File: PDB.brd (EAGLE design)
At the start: 125.9 x 103 mm, 73 parts

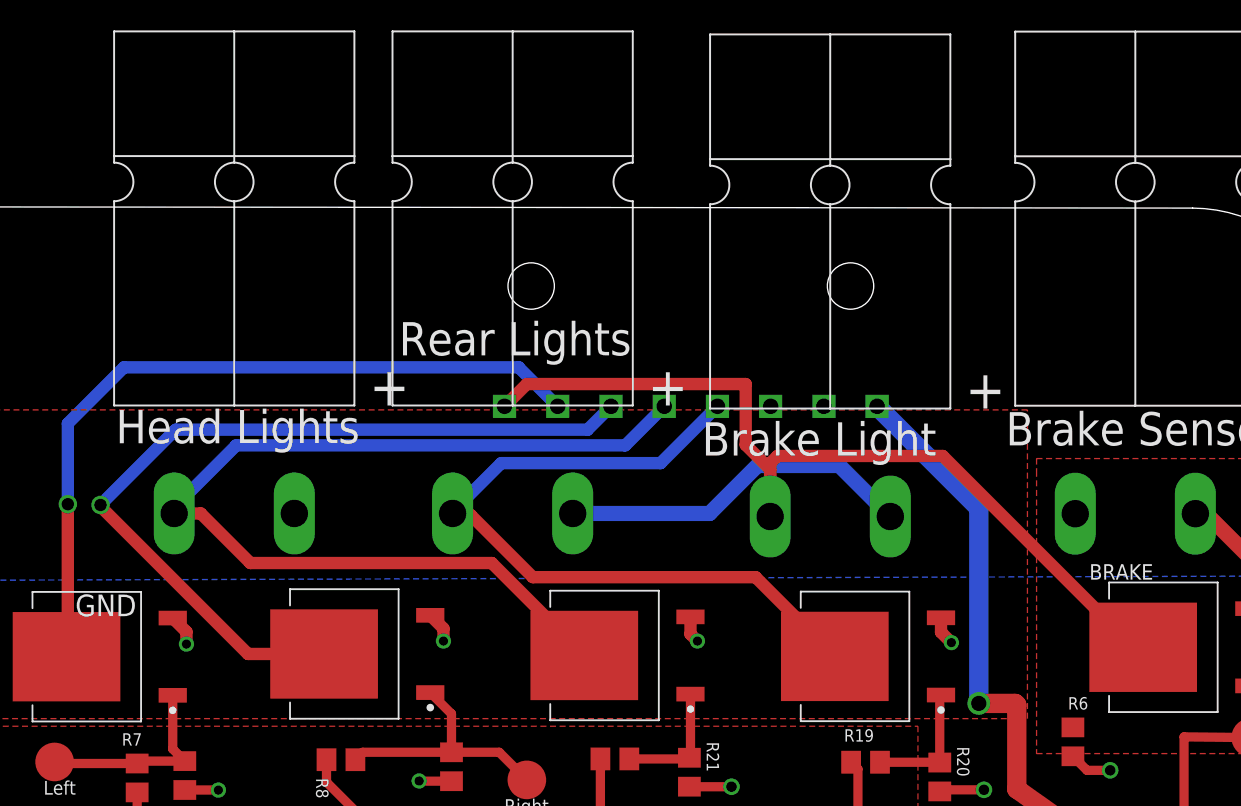
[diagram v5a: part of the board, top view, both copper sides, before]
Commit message: Deleted most Anderson connectors. Brake sensor waiting to be modified
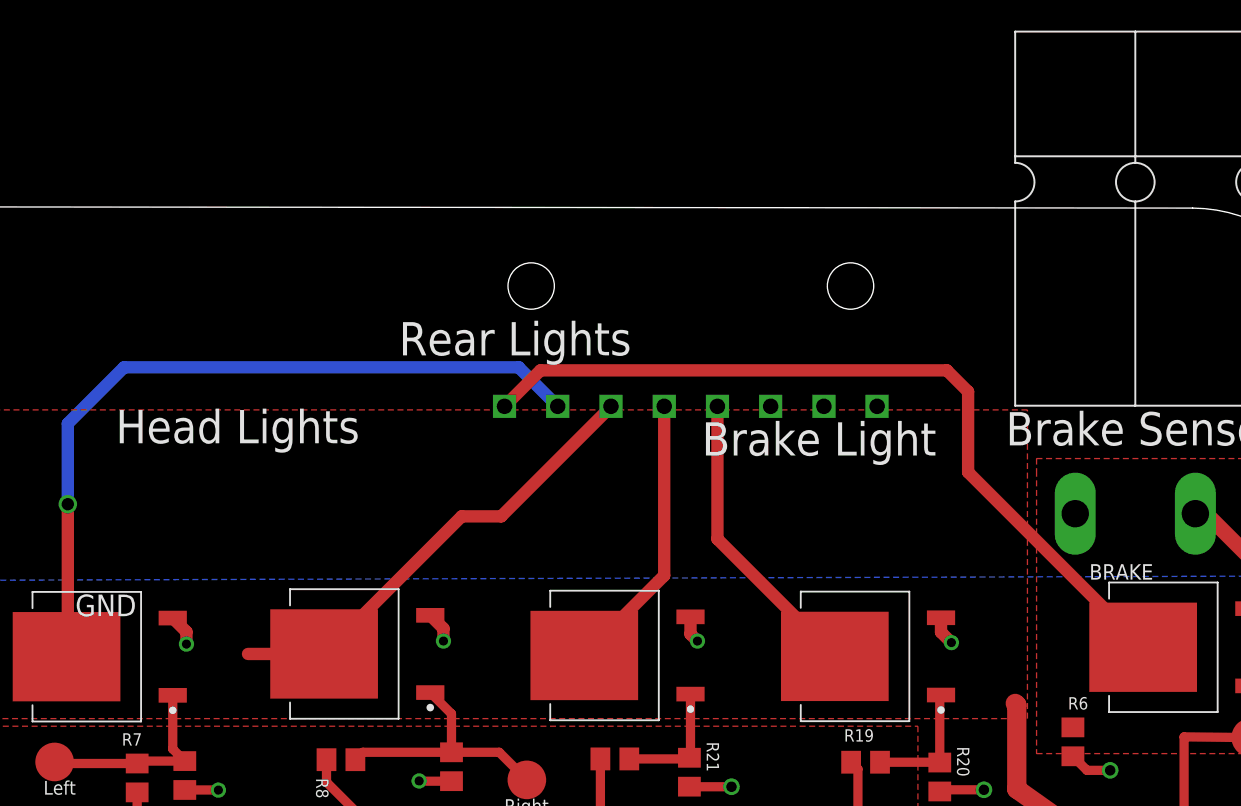
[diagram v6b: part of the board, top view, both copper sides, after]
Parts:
- removed BRAKE_OUT, HEADLIGHTS_OUT, REARLIGHTS_OUT: POWERPOLE_POWER25A_HORIZONTAL_G2, powerpoles:POWERPOLE_PAIR_25A_HORIZ_G2
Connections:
- removed net V+: BRAKE_OUT.RED, REARLIGHTS_OUT.RED
- net BRAKE_SIG: no longer BRAKE_OUT.BLACK
- net HEADLIGHT_SIG: no longer HEADLIGHTS_OUT.BLACK
- net REARLIGHT_SIG: no longer REARLIGHTS_OUT.BLACK
- net VDD: no longer HEADLIGHTS_OUT.RED
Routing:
- net HEADLIGHT_SIG: track 66.2 -> 18.6 mm
- net REARLIGHT_SIG: track 49.4 -> 19.6 mm
- net VDD: track 44.8 -> 20.1 mm, vias 1 -> 0
- net HAZ_R_SIG: track 58.4 -> 33.9 mm, vias 1 -> 0
- net V+: track 23.6 -> 0.00 mm
- net BRAKE_SIG: track 59.3 -> 53.6 mm
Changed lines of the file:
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@@
 <drawing>
 <settings>
-<setting alwaysvectorfont="yes"/>
+<setting alwaysvectorfont="no"/>
 <setting verticaltext="up"/>
 </settings>
@@
 <element name="ADD1" library="master_library" package="TO254P1054X240-3" package3d_urn="urn:adsk.eagle:package:8893803/1" value="NCV8405ADPAK-3PIN" x="56.654" y="68.958" smashed="yes" rot="R270"/>
 <element name="WIPER_OUT" library="powerpoles" package="POWERPOLE_PAIR_25A_HORIZ_G2" value="POWERPOLE_POWER25A_HORIZONTAL_G2" x="35.64" y="51.84" smashed="yes" rot="R180"/>
-<element name="BRAKE_OUT" library="powerpoles" package="POWERPOLE_PAIR_25A_HORIZ_G2" value="POWERPOLE_POWER25A_HORIZONTAL_G2" x="96.232" y="133.49" smashed="yes"/>
-<element name="HEADLIGHTS_OUT" library="powerpoles" package="POWERPOLE_PAIR_25A_HORIZ_G2" value="POWERPOLE_POWER25A_HORIZONTAL_G2" x="57.044" y="133.69" smashed="yes"/>
-<element name="REARLIGHTS_OUT" library="powerpoles" package="POWERPOLE_PAIR_25A_HORIZ_G2" value="POWERPOLE_POWER25A_HORIZONTAL_G2" x="75.35" y="133.69" smashed="yes"/>
 <element name="BRAKE" library="master_library" package="TO254P1054X240-3" package3d_urn="urn:adsk.eagle:package:8893803/1" value="NCV8405ADPAK-3PIN" x="118.994" y="117.792" smashed="yes" rot="R180">
 <attribute name="NAME" x="113.26755" y="122.239" size="1.017" layer="25" font="vector" rot="SR0"/>
@@
 <signals>
 <signal name="VDD">
-<contactref element="HEADLIGHTS_OUT" pad="RED"/>
 <contactref element="C10" pad="+"/>
 <contactref element="D1" pad="C"/>
@@
 <wire x1="108.5" y1="108.461690625" x2="108.5" y2="114" width="1.27" layer="1"/>
 <wire x1="108.5" y1="114" x2="108.4" y2="114.1" width="1.27" layer="1"/>
-<wire x1="108.4" y1="114.1" x2="106" y2="114.1" width="1.27" layer="1"/>
 <wire x1="118.24" y1="101.56" x2="118.236340625" y2="101.57038125" width="1.27" layer="1"/>
-<via x="106" y="114.1" extent="1-16" drill="1"/>
 <contactref element="U$2" pad="P$1"/>
 <contactref element="U$2" pad="P$2"/>
@@
 <contactref element="LIGHTS" pad="P7"/>
 <contactref element="LIGHTS" pad="P8"/>
-<wire x1="106" y1="114.1" x2="106" y2="126.952" width="1.27" layer="16"/>
-<wire x1="106" y1="126.952" x2="99.316" y2="133.636" width="1.27" layer="16"/>
 </signal>
 <signal name="N$19">
@@
 </signal>
 <signal name="BRAKE_SIG">
-<contactref element="BRAKE" pad="3"/>
-<contactref element="BRAKE_OUT" pad="BLACK"/>
 <contactref element="LIGHTS" pad="P1"/>
-<wire x1="103.631" y1="130.37" x2="92.762" y2="130.37" width="0.8128" layer="1"/>
-<wire x1="90.672" y1="131.1" x2="90.672" y2="135.1" width="0.8128" layer="1"/>
-<wire x1="90.672" y1="135.1" x2="76.28" y2="135.1" width="0.8128" layer="1"/>
-<wire x1="92.762" y1="130.37" x2="92.282" y2="129.89" width="0.8128" layer="1"/>
-<wire x1="116.209" y1="117.792" x2="103.631" y2="130.37" width="0.8128" layer="1"/>
-<wire x1="76.28" y1="135.1" x2="74.816" y2="133.636" width="0.8128" layer="1"/>
-<wire x1="92.282" y1="129.49" x2="90.672" y2="131.1" width="0.8128" layer="1"/>
-<wire x1="92.282" y1="129.89" x2="92.282" y2="126.39" width="0.8128" layer="1"/>
-<wire x1="92.282" y1="126.39" x2="92.282" y2="129.49" width="0.8128" layer="1"/>
-<wire x1="116.809" y1="117.792" x2="116.209" y2="117.792" width="0.8128" layer="1"/>
+<contactref element="BRAKE" pad="3"/>
+<wire x1="116.809" y1="117.792" x2="105.3" y2="129.301" width="0.8128" layer="1"/>
+<wire x1="105.3" y1="129.301" x2="105.3" y2="134.6" width="0.8128" layer="1"/>
+<wire x1="105.3" y1="134.6" x2="103.9" y2="136" width="0.8128" layer="1"/>
+<wire x1="77.18" y1="136" x2="74.816" y2="133.636" width="0.8128" layer="1"/>
+<wire x1="103.9" y1="136" x2="77.18" y2="136" width="0.8128" layer="1"/>
 </signal>
 <signal name="HEADLIGHT_SIG">
-<contactref element="HEAD" pad="3"/>
-<contactref element="HEADLIGHTS_OUT" pad="BLACK"/>
 <contactref element="LIGHTS" pad="P4"/>
-<wire x1="85.316" y1="133.636" x2="82.744" y2="131.064" width="0.8128" layer="16"/>
-<wire x1="82.744" y1="131.064" x2="57.164" y2="131.064" width="0.8128" layer="16"/>
-<wire x1="57.164" y1="131.064" x2="53.094" y2="126.994" width="0.8128" layer="16"/>
-<wire x1="53.094" y1="126.994" x2="53.094" y2="126.59" width="0.8128" layer="16"/>
-<wire x1="80.061" y1="117.252" x2="73.9818" y2="123.3312" width="0.8128" layer="1"/>
-<wire x1="54.84454375" y1="126.59" x2="53.094" y2="126.59" width="0.8128" layer="1"/>
-<wire x1="58.10334375" y1="123.3312" x2="54.84454375" y2="126.59" width="0.8128" layer="1"/>
-<wire x1="73.9818" y1="123.3312" x2="58.10334375" y2="123.3312" width="0.8128" layer="1"/>
+<contactref element="HEAD" pad="3"/>
+<wire x1="80.061" y1="117.252" x2="85.316" y2="122.507" width="0.8128" layer="1"/>
+<wire x1="85.316" y1="122.507" x2="85.316" y2="133.636" width="0.8128" layer="1"/>
 </signal>
 <signal name="REARLIGHT_SIG">
-<contactref element="REAR" pad="3"/>
-<contactref element="REARLIGHTS_OUT" pad="BLACK"/>
 <contactref element="LIGHTS" pad="P5"/>
-<wire x1="88.816" y1="133.636" x2="85.08" y2="129.9" width="0.8128" layer="16"/>
-<wire x1="85.08" y1="129.9" x2="74.6" y2="129.9" width="0.8128" layer="16"/>
-<wire x1="74.6" y1="129.9" x2="71.4" y2="126.7" width="0.8128" layer="16"/>
-<wire x1="71.4" y1="126.7" x2="71.4" y2="126.59" width="0.8128" layer="16"/>
-<wire x1="96.535" y1="117.192" x2="91.327" y2="122.4" width="0.8128" layer="1"/>
-<wire x1="76.678" y1="122.4" x2="72.588" y2="126.49" width="0.8128" layer="1"/>
-<wire x1="91.327" y1="122.4" x2="76.678" y2="122.4" width="0.8128" layer="1"/>
-<wire x1="72.588" y1="126.49" x2="71.5" y2="126.49" width="0.8128" layer="1"/>
-<wire x1="71.5" y1="126.49" x2="71.4" y2="126.59" width="0.8128" layer="1"/>
+<contactref element="REAR" pad="3"/>
+<wire x1="96.535" y1="117.192" x2="88.816" y2="124.911" width="0.8128" layer="1"/>
+<wire x1="88.816" y1="124.911" x2="88.816" y2="133.636" width="0.8128" layer="1"/>
 </signal>
 <signal name="H3">
@@
 <wire x1="62.951" y1="117.352" x2="59.648" y2="117.352" width="0.8128" layer="1"/>
 <wire x1="62.951" y1="117.352" x2="57.948" y2="117.352" width="0.8128" layer="1"/>
-<wire x1="57.948" y1="117.352" x2="48.2" y2="127.1" width="0.8128" layer="1"/>
-<wire x1="48.2" y1="127.1" x2="48.25" y2="127.15" width="0.8128" layer="1"/>
-<via x="48.25" y="127.15" extent="1-16" drill="0.8128"/>
-<wire x1="48.25" y1="127.15" x2="53.2" y2="132.1" width="0.8128" layer="16"/>
-<wire x1="53.2" y1="132.1" x2="80.28" y2="132.1" width="0.8128" layer="16"/>
-<wire x1="80.28" y1="132.1" x2="81.816" y2="133.636" width="0.8128" layer="16"/>
+<wire x1="62.951" y1="117.352" x2="71.999" y2="126.4" width="0.8128" layer="1"/>
+<wire x1="71.999" y1="126.4" x2="74.6" y2="126.4" width="0.8128" layer="1"/>
+<wire x1="74.6" y1="126.4" x2="81.816" y2="133.616" width="0.8128" layer="1"/>
+<wire x1="81.816" y1="133.616" x2="81.816" y2="133.636" width="0.8128" layer="1"/>
 </signal>
 <signal name="EXT_CLK">
@@
 <wire x1="113" y1="100.55" x2="112.9896" y2="100.5396" width="1.016" layer="1"/>
 </signal>
-<signal name="V+">
-<contactref element="BRAKE_OUT" pad="RED"/>
-<contactref element="REARLIGHTS_OUT" pad="RED"/>
-<wire x1="79.3" y1="126.59" x2="88.300175" y2="126.59" width="1" layer="16"/>
-<wire x1="88.300175" y1="126.59" x2="91.452575" y2="129.7424" width="1" layer="16"/>
-<wire x1="91.452575" y1="129.7424" x2="96.8296" y2="129.7424" width="1" layer="16"/>
-<wire x1="96.8296" y1="129.7424" x2="100.182" y2="126.39" width="1" layer="16"/>
-</signal>
 </signals>

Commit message: adds new connectors and relays, and removes old connectors and wiper fet
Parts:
- removed 555: LM555N, linear:DIL08
- removed C1: 33uF, rcl:C0805
- removed C10, C4: 22uF, SparkFun-Capacitors:PANASONIC_C
- removed C2: 0.01uF, rcl:C0805
- removed C3: 10uF, rcl:C0805
- removed D1: 15V, diode:DO41Z10
- removed D2: 1N4446, diode:DO35-10
- removed R10: 1K, rcl:R0805
- removed R11: 10K, pot:B25U
- removed R14: 220, rcl:R0805
- removed R15: 5K, rcl:R0805
- removed R3: 4.7K, rcl:R0805
- removed TP1, TP4: PTR1B2,54, testpad:B2,54
- removed VDD_IN, VDD_IN1, WIPER_OUT: POWERPOLE_POWER25A_HORIZONTAL_G2, powerpoles:POWERPOLE_PAIR_25A_HORIZ_G2
- removed WIPER_: NCV8405ADPAK-3PIN, master_library:TO254P1054X240-3
- added HORN: (no value), switch:M9040P
- added J1, J2, J5: B06B-HCMKK, AUX Lib:B06BHCMKK
- added J3, J4: SS-6488-NF-A431, AUX Lib:SS6488NFA431
- added J6, J7: B03B-HCMKS, AUX Lib:B03BHCMKS
- added POWER1: (no value), led:CHIPLED_0805
- added R1: 470, resistor:R3225
- added U$3: (no value), AUX Lib:TEENSY-3.6_ONLY_HOLES
- added U$4: KEYSTONE_FUSE_3522, AUX Lib:KEYSTONE_FUSE_3522
- added U$5, U$6: TE_CON_OJE-SH-112DM,095\, AUX Lib:TE_CON_OJE-SH-112DM,095
- U$2: value BLADEFUSE -> KEYSTONE_FUSE_3522; device master_library:BLADEFUSE -> AUX Lib:KEYSTONE_FUSE_3522
- moved U$2 106.8 mm to (-40.5, -17.2), turned to 0 degrees
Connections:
- removed net 12V_IN: U$2.P$3, U$2.P$4, VDD_IN.RED
- removed net BRAKE_SNS_OUT: BRAKE.1, R6.1, TP7.TP, U$1.P1, VDD_IN1.BLACK
- removed net CV: 555.5, C2.1
- removed net DIS: 555.7, R10.1, R15.1
- removed net N$19: D2.A, WIPER_.3, WIPER_OUT.BLACK
- removed net N$22: R14.2, R3.1, TP4.TP, WIPER_.1
- removed net N$6: R11.A, R15.2
- removed net TR/THR: 555.6, C3.1, R11.S
- new net 3.3V: J3.1, J4.1
- new net 3V3: U$3.3V3_1
- new net 5V: J7.1
- new net AGND: U$3.AGND
- new net BRAKE_SNS: BRAKE.1, J6.2, R6.1, TP7.TP, U$1.P1
- new net CLK_A: J3.4
- new net CLK_B: J4.4
- new net H9: HORN.1, U$5.CLA
- new net HORN: U$5.SWB
- new net IGND: J2.6, J5.5, R1.2
- new net ISOENABLE: J5.3
- new net IVDD: J2.1, POWER1.A, U$4.B1, U$4.B2, U$5.SWA, U$6.SWA
- new net MISO_A: J3.5
- new net MISO_B: J4.5
- new net MOSI_A: J3.3
- new net MOSI_B: J4.3
- new net N$10: POWER1.C, R1.1
- new net N$7: J5.1, U$2.B1, U$2.B2
- new net N$8: J5.2, U$4.A1, U$4.A2
- new net PEDAL_SNS: J7.2
- new net WIPER: U$6.SWB
- net 10V_REG: now also HORN.2; no longer 555.4, 555.8, C4.+, R10.2
- net 555_OUT: no longer TP1.TP
- net 5V_REG: now also J6.1, U$3.VIN; no longer VDD_IN1.RED
- net GND: now also J1.6, J3.2, J4.2, J5.6, J7.3, U$3.GND1, U$3.GND2, U$5.CLB, U$6.CLB; no longer 555.1, C1.2, C10.-, C2.2, C3.2, C4.-, D1.A, R3.2, VDD_IN.BLACK, WIPER_.2
- net H4: now also U$6.CLA; no longer R14.1
- net VDD: now also ADD1.3, J1.1, U$2.A1, U$2.A2; no longer C10.+, D1.C, D2.C, U$2.P$1, U$2.P$2, WIPER_OUT.RED
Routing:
- net BRAKE_SNS_OUT: track 86.2 -> 0.00 mm, vias 1 -> 0
- net BRAKE_SNS: track 0.00 -> 86.2 mm, vias 0 -> 1
- net TR/THR: track 29.6 -> 0.00 mm
- net GND: track 89.7 -> 70.2 mm, vias 20 -> 14
- net N$22: track 17.7 -> 0.00 mm
- net DIS: track 14.3 -> 0.00 mm
- net N$19: track 13.8 -> 0.00 mm
- net 10V_REG: track 6.12 -> 0.00 mm
- net CV: track 3.62 -> 0.00 mm
- net N$6: track 3.12 -> 0.00 mm
- net 555_OUT: track 29.3 -> 27.3 mm
- net H4: track 10.1 -> 8.35 mm
- net 5V_REG: track 33.7 -> 33.0 mm
- added copper zone on layer 1, net BRAKE_SNS
- removed copper zone on layer 1, net BRAKE_SNS_OUT

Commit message: Schemetic first draft done
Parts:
- removed 555_CLK_LED, _ADD1, _ADD2, _EXT_CLK: (no value), led:CHIPLED_0805
- removed ADD1: NCV8405ADPAK-3PIN, master_library:TO254P1054X240-3
- removed ADD1_: (no value), switch:M9040P
- removed JP2: (no value), jumper:JP2
- removed LIGHTS: 8-PIN-MOLEX-RA-FEMALE, master_library:8-PIN-MOLEX
- removed R13: 220, rcl:R0805
- removed R17: 470, resistor:R3225
- removed R2: 4.7K, rcl:R0805
- removed R23: 100, resistor:R0805
- removed R24, R25: 710, master_library:R0805
- removed TP3: PTR1B2,54, testpad:B2,54
- removed U$1: JST-PH_5-PIN_HEADER, master_library:JST_B5B-PH_HEADER
- added J8: SS-6488-NF-A431, AUX Lib:SS6488NFA431
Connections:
- removed net 3V3: U$3.3V3_1
- removed net 555_OUT: 555_CLK_LED.A, JP2.1
- removed net EXT_CLK: JP2.3, U$1.P2, _EXT_CLK.A
- removed net H5: ADD1_.2, R13.1
- removed net N$2: 555_CLK_LED.C, R17.1
- removed net N$26: ADD1.1, R13.2, R2.1, TP3.TP
- removed net N$3: R23.1, _EXT_CLK.C
- removed net N$4: R24.1, _ADD1.C
- removed net N$5: R25.1, _ADD2.C
- removed net µC_ADD_1: ADD1_.1, U$1.P4, _ADD1.A
- removed net µC_ADD_2: U$1.P3, _ADD2.A
- new net CLK_SW: J8.4, U$3.2
- new net CS: J8.6, U$3.4
- new net DC: J8.5, U$3.5
- new net MOSI_SW: J8.3, U$3.3
- new net RESET: J8.7, U$3.6
- net 10V_REG: no longer ADD1_.3
- net 3.3V: now also U$3.3V3_1
- net 5V_REG: now also J8.1
- net BRAKE_SIG: now also J2.2; no longer LIGHTS.P1
- net BRAKE_SNS: now also U$3.17; no longer U$1.P1
- net CLK: now also U$3.14; no longer JP2.2
- net CLK_A: now also U$3.32
- net CLK_B: now also U$3.13
- net GND: now also J8.2; no longer ADD1.2, R17.2, R2.2
- net HAZ_L_SIG: now also J1.2; no longer LIGHTS.P2
- net HAZ_R_SIG: now also J1.3; no longer LIGHTS.P3
- net HEADLIGHT_SIG: now also J1.4; no longer LIGHTS.P4
- net ISOENABLE: now also U$3.38
- net MISO_A: now also U$3.1
- net MISO_B: now also U$3.12
- net MOSI_A: now also U$3.0
- net MOSI_B: now also U$3.11
- net PEDAL_SNS: now also U$3.39
- net REARLIGHT_SIG: now also J1.5; no longer LIGHTS.P5
- net VDD: no longer ADD1.3, LIGHTS.P6, LIGHTS.P7, LIGHTS.P8
- net µC_GND: no longer R23.2, R24.2, R25.2, U$1.P5
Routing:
- net µC_ADD_1: track 76.4 -> 0.00 mm, vias 1 -> 0
- net EXT_CLK: track 69.4 -> 0.00 mm, vias 2 -> 0
- net 555_OUT: track 27.3 -> 0.00 mm, vias 1 -> 0
- net µC_ADD_2: track 18.0 -> 0.00 mm
- net N$26: track 16.8 -> 0.00 mm
- net CLK: track 15.1 -> 0.82 mm
- net GND: track 70.2 -> 58.7 mm, vias 14 -> 11
- net HEADLIGHT_SIG: track 18.6 -> 7.43 mm
- net REARLIGHT_SIG: track 19.6 -> 10.9 mm
- net µC_GND: track 20.8 -> 13.4 mm, vias 3 -> 0
- net H5: track 6.96 -> 0.00 mm
- net N$2: track 5.66 -> 0.00 mm
- net N$5: track 5.00 -> 0.00 mm
- net N$3: track 4.88 -> 0.00 mm
- net N$4: track 4.82 -> 0.00 mm
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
